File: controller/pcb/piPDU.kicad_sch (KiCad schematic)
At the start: 26 parts, among them J0 SCR_5V, J1 SCR_BTN_1, J10 SCR_BTN_10, J11 SCR_BTN_11, J12 SCR_BTN_12, J13 SCR_BTN_13, J14 SCR_BTN_14, J15 SCR_BTN_15, J16 SCR_BTN_16, J2 SCR_BTN_2, J3 SCR_BTN_3, J35 Raspberry_Pi_2_3, J4 SCR_BTN_4, J5 SCR_BTN_5, J6 SCR_BTN_6, J7 SCR_BTN_7, J8 SCR_BTN_8, J9 SCR_BTN_9, U1 PCF8574, U2 PCF8574, U3 PCF8574, U4 PCF8574, U5 8P_Header, U6 8P_Header, U7 8P_Header, U8 8P_Header

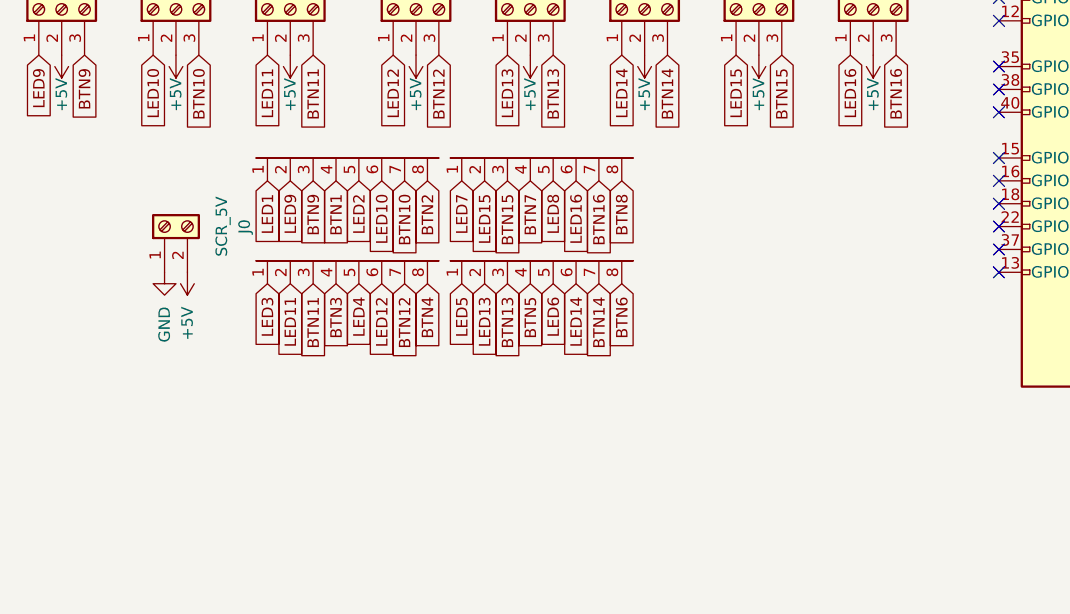
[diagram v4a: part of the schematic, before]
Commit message: Update controller pcb and schematic to use GPIO expanders
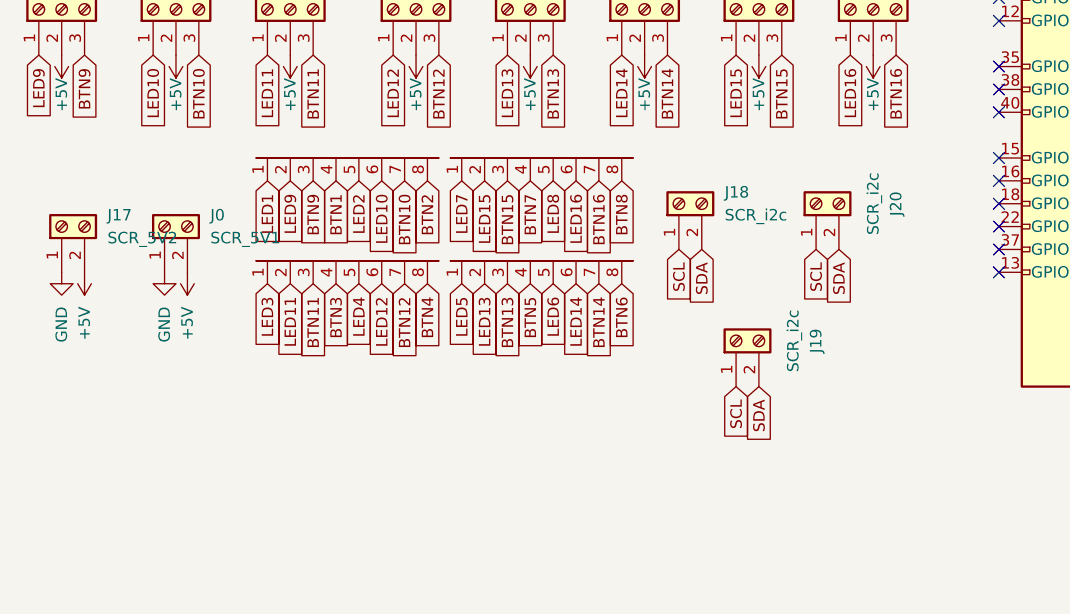
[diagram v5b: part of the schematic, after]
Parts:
- added J17: SCR_5V2, TerminalBlock:TerminalBlock_bornier-2_P5.08mm, symbol Connector:Screw_Terminal_01x02
- added J18, J19, J20: SCR_i2c, TerminalBlock:TerminalBlock_bornier-2_P5.08mm, symbol Connector:Screw_Terminal_01x02
- J0: value SCR_5V -> SCR_5V1
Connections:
- net +5V: now also J17.2 (Pin_2)
- net GND: now also J17.1 (Pin_1)
- net SCL: now also J18.1 (Pin_1), J19.1 (Pin_1), J20.1 (Pin_1)
- net SDA: now also J18.2 (Pin_2), J19.2 (Pin_2), J20.2 (Pin_2)
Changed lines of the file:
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@@
+    )
+  )
+  (global_label "SCL" (shape input) (at 100.33 64.77 270) (fields_autoplaced)
+    (effects (font (size 1.27 1.27)) (justify right))
+    (property "Intersheet References" "${INTERSHEET_REFS}" (id 0) (at 100.4094 70.6907 90)
+      (effects (font (size 1.27 1.27)) (justify right) hide)
     )
   )
@@
     )
   )
+  (global_label "SDA" (shape input) (at 102.87 64.77 270) (fields_autoplaced)
+    (effects (font (size 1.27 1.27)) (justify right))
+    (property "Intersheet References" "${INTERSHEET_REFS}" (id 0) (at 102.9494 70.7512 90)
+      (effects (font (size 1.27 1.27)) (justify right) hide)
+    )
+  )
+  (global_label "SCL" (shape input) (at 91.44 80.01 270) (fields_autoplaced)
+    (effects (font (size 1.27 1.27)) (justify right))
+    (property "Intersheet References" "${INTERSHEET_REFS}" (id 0) (at 91.5194 85.9307 90)
+      (effects (font (size 1.27 1.27)) (justify right) hide)
+    )
+  )
   (global_label "SDA" (shape input) (at 175.26 26.67 180) (fields_autoplaced)
     (effects (font (size 1.27 1.27)) (justify right))
@@
     )
   )
+  (global_label "SDA" (shape input) (at 87.63 64.77 270) (fields_autoplaced)
+    (effects (font (size 1.27 1.27)) (justify right))
+    (property "Intersheet References" "${INTERSHEET_REFS}" (id 0) (at 87.7094 70.7512 90)
+      (effects (font (size 1.27 1.27)) (justify right) hide)
+    )
+  )
   (global_label "LED7" (shape input) (at 91.44 24.13 270) (fields_autoplaced)
     (effects (font (size 1.27 1.27)) (justify right))
@@
     (effects (font (size 1.27 1.27)) (justify right))
     (property "Intersheet References" "${INTERSHEET_REFS}" (id 0) (at 39.2906 64.2198 90)
+      (effects (font (size 1.27 1.27)) (justify right) hide)
+    )
+  )
+  (global_label "SDA" (shape input) (at 93.98 80.01 270) (fields_autoplaced)
+    (effects (font (size 1.27 1.27)) (justify right))
+    (property "Intersheet References" "${INTERSHEET_REFS}" (id 0) (at 94.0594 85.9912 90)
+      (effects (font (size 1.27 1.27)) (justify right) hide)
+    )
+  )
+  (global_label "SCL" (shape input) (at 85.09 64.77 270) (fields_autoplaced)
+    (effects (font (size 1.27 1.27)) (justify right))
+    (property "Intersheet References" "${INTERSHEET_REFS}" (id 0) (at 85.1694 70.6907 90)
       (effects (font (size 1.27 1.27)) (justify right) hide)
     )
@@
     (pin "7")
     (pin "8")
+  )
+  (symbol (lib_id "Connector:Screw_Terminal_01x02") (at 16.51 62.23 90) (unit 1)
+    (in_bom yes) (on_board yes) (fields_autoplaced)
+    (property "Reference" "J17" (id 0) (at 21.59 60.9599 90)
+      (effects (font (size 1.27 1.27)) (justify right))
+    )
+    (property "Value" "SCR_5V2" (id 1) (at 21.59 63.4999 90)
+      (effects (font (size 1.27 1.27)) (justify right))
+    )
+    (property "Footprint" "TerminalBlock:TerminalBlock_bornier-2_P5.08mm" (id 2) (at 16.51 62.23 0)
+      (effects (font (size 1.27 1.27)) hide)
+    )
+    (property "Datasheet" "~" (id 3) (at 16.51 62.23 0)
+      (effects (font (size 1.27 1.27)) hide)
+    )
+    (pin "1")
+    (pin "2")
   )
   (symbol (lib_id "Connector:Screw_Terminal_01x03") (at 81.28 38.1 90) (unit 1)
@@
   )
   (symbol (lib_id "Connector:Screw_Terminal_01x02") (at 27.94 62.23 90) (unit 1)
-    (in_bom yes) (on_board yes) (fields_autoplaced)
-    (property "Reference" "J0" (id 0) (at 36.83 62.23 0))
-    (property "Value" "SCR_5V" (id 1) (at 34.29 62.23 0))
+    (in_bom yes) (on_board yes)
+    (property "Reference" "J0" (id 0) (at 33.02 60.9599 90)
+      (effects (font (size 1.27 1.27)) (justify right))
+    )
+    (property "Value" "SCR_5V1" (id 1) (at 33.02 63.4999 90)
+      (effects (font (size 1.27 1.27)) (justify right))
+    )
     (property "Footprint" "TerminalBlock:TerminalBlock_bornier-2_P5.08mm" (id 2) (at 27.94 62.23 0)
       (effects (font (size 1.27 1.27)) hide)
@@
     (pin "1")
   )
+  (symbol (lib_id "power:+5V") (at 19.05 67.31 180) (unit 1)
+    (in_bom yes) (on_board yes) (fields_autoplaced)
+    (property "Reference" "#PWR0114" (id 0) (at 19.05 63.5 0)
+      (effects (font (size 1.27 1.27)) hide)
+    )
+    (property "Value" "+5V" (id 1) (at 19.0501 71.12 90)
+      (effects (font (size 1.27 1.27)) (justify left))
+    )
+    (property "Footprint" "" (id 2) (at 19.05 67.31 0)
+      (effects (font (size 1.27 1.27)) hide)
+    )
+    (property "Datasheet" "" (id 3) (at 19.05 67.31 0)
+      (effects (font (size 1.27 1.27)) hide)
+    )
+    (pin "1")
+  )
   (symbol (lib_id "Connector:Screw_Terminal_01x03") (at 29.21 19.05 90) (unit 1)
     (in_bom yes) (on_board yes)
@@
     )
     (pin "1")
+  )
+  (symbol (lib_id "Connector:Screw_Terminal_01x02") (at 85.09 59.69 90) (unit 1)
+    (in_bom yes) (on_board yes)
+    (property "Reference" "J18" (id 0) (at 90.17 58.4199 90)
+      (effects (font (size 1.27 1.27)) (justify right))
+    )
+    (property "Value" "SCR_i2c" (id 1) (at 90.17 60.96 90)
+      (effects (font (size 1.27 1.27)) (justify right))
+    )
+    (property "Footprint" "TerminalBlock:TerminalBlock_bornier-2_P5.08mm" (id 2) (at 85.09 59.69 0)
+      (effects (font (size 1.27 1.27)) hide)
+    )
+    (property "Datasheet" "~" (id 3) (at 85.09 59.69 0)
+      (effects (font (size 1.27 1.27)) hide)
+    )
+    (pin "1")
+    (pin "2")
   )
   (symbol (lib_id "Interface_Expansion:PCF8574") (at 187.96 81.28 0) (unit 1)
@@
     (pin "1")
   )
+  (symbol (lib_id "power:GND") (at 16.51 67.31 0) (unit 1)
+    (in_bom yes) (on_board yes) (fields_autoplaced)
+    (property "Reference" "#PWR0122" (id 0) (at 16.51 73.66 0)
+      (effects (font (size 1.27 1.27)) hide)
+    )
+    (property "Value" "GND" (id 1) (at 16.5101 71.12 90)
+      (effects (font (size 1.27 1.27)) (justify right))
+    )
+    (property "Footprint" "" (id 2) (at 16.51 67.31 0)
+      (effects (font (size 1.27 1.27)) hide)
+    )
+    (property "Datasheet" "" (id 3) (at 16.51 67.31 0)
+      (effects (font (size 1.27 1.27)) hide)
+    )
+    (pin "1")
+  )
   (symbol (lib_id "Connector:Screw_Terminal_01x03") (at 41.91 38.1 90) (unit 1)
     (in_bom yes) (on_board yes)
@@
     (pin "2")
     (pin "3")
+  )
+  (symbol (lib_id "Connector:Screw_Terminal_01x02") (at 100.33 59.69 90) (unit 1)
+    (in_bom yes) (on_board yes) (fields_autoplaced)
+    (property "Reference" "J20" (id 0) (at 109.22 59.69 0))
+    (property "Value" "SCR_i2c" (id 1) (at 106.68 59.69 0))
+    (property "Footprint" "TerminalBlock:TerminalBlock_bornier-2_P5.08mm" (id 2) (at 100.33 59.69 0)
+      (effects (font (size 1.27 1.27)) hide)
+    )
+    (property "Datasheet" "~" (id 3) (at 100.33 59.69 0)
+      (effects (font (size 1.27 1.27)) hide)
+    )
+    (pin "1")
+    (pin "2")
   )
   (symbol (lib_id "power:+5V") (at 106.68 24.13 180) (unit 1)
@@
     (pin "1")
   )
+  (symbol (lib_id "Connector:Screw_Terminal_01x02") (at 91.44 74.93 90) (unit 1)
+    (in_bom yes) (on_board yes) (fields_autoplaced)
+    (property "Reference" "J19" (id 0) (at 100.33 74.93 0))
+    (property "Value" "SCR_i2c" (id 1) (at 97.79 74.93 0))
+    (property "Footprint" "TerminalBlock:TerminalBlock_bornier-2_P5.08mm" (id 2) (at 91.44 74.93 0)
+      (effects (font (size 1.27 1.27)) hide)
+    )
+    (property "Datasheet" "~" (id 3) (at 91.44 74.93 0)
+      (effects (font (size 1.27 1.27)) hide)
+    )
+    (pin "1")
+    (pin "2")
+  )
   (sheet_instances
     (path "/" (page "1"))
@@
       (reference "#PWR0113") (unit 1) (value "GND") (footprint "")
     )
+    (path "/a6d1f81e-be6f-4a49-8717-0f9019c653f6"
+      (reference "#PWR0114") (unit 1) (value "+5V") (footprint "")
+    )
     (path "/90411737-b8b6-4330-9d77-11ab3901de4a"
       (reference "#PWR0115") (unit 1) (value "+5V") (footprint "")
@@
       (reference "#PWR0121") (unit 1) (value "+5V") (footprint "")
     )
+    (path "/defe84e1-d8b8-4d3a-9e6e-9c015d24a3f0"
+      (reference "#PWR0122") (unit 1) (value "GND") (footprint "")
+    )
     (path "/ead94fbb-2897-4198-a875-67cbb9a3350d"
       (reference "#PWR0123") (unit 1) (value "+5V") (footprint "")
@@
     )
     (path "/579f3f6a-2e9b-46c5-a3ed-fba904d359a8"
-      (reference "J0") (unit 1) (value "SCR_5V") (footprint "TerminalBlock:TerminalBlock_bornier-2_P5.08mm")
+      (reference "J0") (unit 1) (value "SCR_5V1") (footprint "TerminalBlock:TerminalBlock_bornier-2_P5.08mm")
     )
     (path "/fbb12e1e-9934-4147-b341-44c35de2a632"
@@
       (reference "J16") (unit 1) (value "SCR_BTN_16") (footprint "TerminalBlock:TerminalBlock_bornier-3_P5.08mm")
     )
+    (path "/083cd636-4a29-489d-bf54-ee7e897cd5cb"
+      (reference "J17") (unit 1) (value "SCR_5V2") (footprint "TerminalBlock:TerminalBlock_bornier-2_P5.08mm")
+    )
+    (path "/b050743d-0659-427c-add9-932c058055ef"
+      (reference "J18") (unit 1) (value "SCR_i2c") (footprint "TerminalBlock:TerminalBlock_bornier-2_P5.08mm")
+    )
+    (path "/febbd446-67aa-49c6-a7de-46c3aaac01d0"
+      (reference "J19") (unit 1) (value "SCR_i2c") (footprint "TerminalBlock:TerminalBlock_bornier-2_P5.08mm")
+    )
+    (path "/f6540eaf-4263-4fc5-a16b-73d442daf244"
+      (reference "J20") (unit 1) (value "SCR_i2c") (footprint "TerminalBlock:TerminalBlock_bornier-2_P5.08mm")
+    )
     (path "/81a8b50f-5422-4702-aa19-287baed0af0c"
